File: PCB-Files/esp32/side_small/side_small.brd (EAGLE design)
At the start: 20 x 17 mm, 11 parts

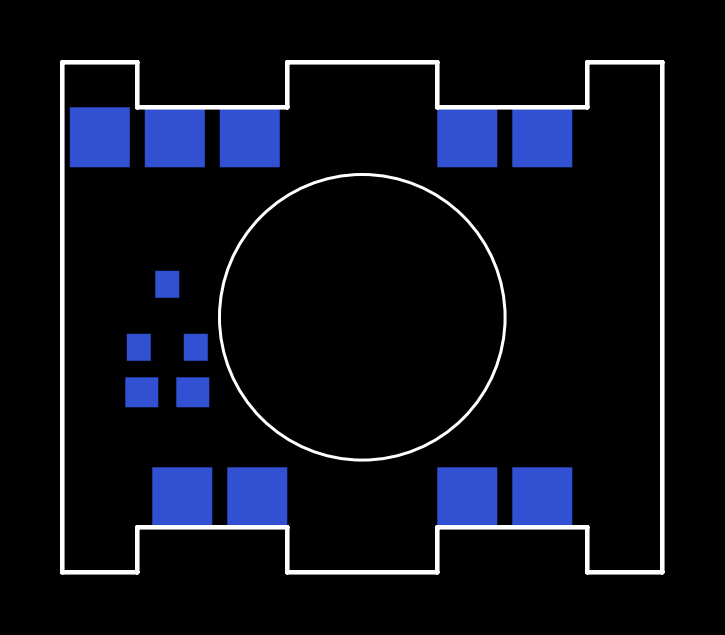
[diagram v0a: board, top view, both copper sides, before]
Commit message: basic layout; dimension for toothed joints
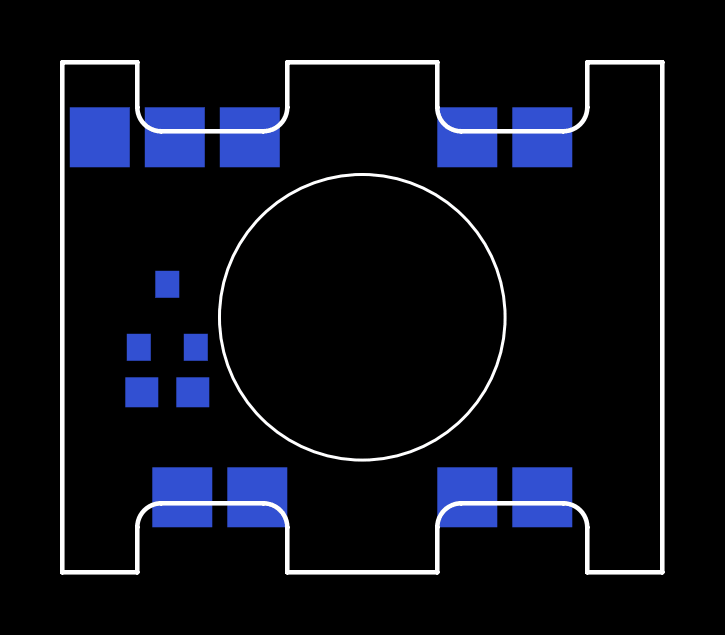
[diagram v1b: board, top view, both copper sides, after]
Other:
- outline, holes or cut-outs redrawn
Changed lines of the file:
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@@
 <board>
 <plain>
-<wire x1="35" y1="17" x2="32.5" y2="17" width="0.1524" layer="20"/>
 <circle x="25" y="8.5" radius="4.76" width="0.1" layer="20"/>
-<wire x1="27.5" y1="17" x2="22.5" y2="17" width="0.1524" layer="20"/>
-<wire x1="17.5" y1="17" x2="15" y2="17" width="0.1524" layer="20"/>
-<wire x1="17.5" y1="17" x2="17.5" y2="15.5" width="0.1524" layer="20"/>
-<wire x1="17.5" y1="15.5" x2="22.5" y2="15.5" width="0.1524" layer="20"/>
-<wire x1="22.5" y1="15.5" x2="22.5" y2="17" width="0.1524" layer="20"/>
-<wire x1="27.5" y1="17" x2="27.5" y2="15.5" width="0.1524" layer="20"/>
-<wire x1="27.5" y1="15.5" x2="32.5" y2="15.5" width="0.1524" layer="20"/>
-<wire x1="32.5" y1="15.5" x2="32.5" y2="17" width="0.1524" layer="20"/>
 <dimension x1="15" y1="17" x2="35" y2="17" x3="25" y3="18.5" textsize="1.778" layer="47"/>
 <wire x1="15" y1="17" x2="15" y2="0" width="0.1524" layer="20"/>
 <wire x1="35" y1="0" x2="35" y2="17" width="0.1524" layer="20"/>
-<wire x1="15" y1="0" x2="17.5" y2="0" width="0.1524" layer="20"/>
-<wire x1="22.5" y1="0" x2="27.5" y2="0" width="0.1524" layer="20"/>
-<wire x1="32.5" y1="0" x2="35" y2="0" width="0.1524" layer="20"/>
-<wire x1="32.5" y1="0" x2="32.5" y2="1.5" width="0.1524" layer="20"/>
-<wire x1="32.5" y1="1.5" x2="27.5" y2="1.5" width="0.1524" layer="20"/>
-<wire x1="27.5" y1="1.5" x2="27.5" y2="0" width="0.1524" layer="20"/>
-<wire x1="22.5" y1="0" x2="22.5" y2="1.5" width="0.1524" layer="20"/>
-<wire x1="22.5" y1="1.5" x2="17.5" y2="1.5" width="0.1524" layer="20"/>
-<wire x1="17.5" y1="1.5" x2="17.5" y2="0" width="0.1524" layer="20"/>
 <dimension x1="35" y1="0" x2="35" y2="17" x3="42" y3="8.5" textsize="1.778" layer="47"/>
 <dimension x1="32.5" y1="15.5" x2="32.5" y2="1.5" x3="38" y3="8.5" textsize="1.778" layer="47"/>
+<wire x1="21.7" y1="14.7" x2="18.3" y2="14.7" width="0.1524" layer="20"/>
+<wire x1="15" y1="17" x2="17.5" y2="17" width="0.1524" layer="20"/>
+<wire x1="17.5" y1="17" x2="17.5" y2="15.5" width="0.1524" layer="20"/>
+<wire x1="22.5" y1="15.5" x2="22.5" y2="17" width="0.1524" layer="20"/>
+<wire x1="22.5" y1="17" x2="27.5" y2="17" width="0.1524" layer="20"/>
+<wire x1="28.3" y1="14.7" x2="27.5" y2="15.5" width="0.1524" layer="20" curve="-90"/>
+<wire x1="27.5" y1="15.5" x2="27.5" y2="17" width="0.1524" layer="20"/>
+<wire x1="32.5" y1="17" x2="32.5" y2="15.5" width="0.1524" layer="20"/>
+<wire x1="32.5" y1="15.5" x2="31.7" y2="14.7" width="0.1524" layer="20" curve="-90"/>
+<wire x1="31.7" y1="14.7" x2="28.3" y2="14.7" width="0.1524" layer="20"/>
+<wire x1="18.3" y1="14.7" x2="17.5" y2="15.5" width="0.1524" layer="20" curve="-90"/>
+<wire x1="22.5" y1="15.5" x2="21.7" y2="14.7" width="0.1524" layer="20" curve="-90"/>
+<wire x1="32.5" y1="17" x2="35" y2="17" width="0.1524" layer="20"/>
+<wire x1="28.3" y1="2.3" x2="31.7" y2="2.3" width="0.1524" layer="20"/>
+<wire x1="35" y1="0" x2="32.5" y2="0" width="0.1524" layer="20"/>
+<wire x1="32.5" y1="0" x2="32.5" y2="1.5" width="0.1524" layer="20"/>
+<wire x1="27.5" y1="1.5" x2="27.5" y2="0" width="0.1524" layer="20"/>
+<wire x1="27.5" y1="0" x2="22.5" y2="0" width="0.1524" layer="20"/>
+<wire x1="21.7" y1="2.3" x2="22.5" y2="1.5" width="0.1524" layer="20" curve="-90"/>
+<wire x1="22.5" y1="1.5" x2="22.5" y2="0" width="0.1524" layer="20"/>
+<wire x1="17.5" y1="0" x2="17.5" y2="1.5" width="0.1524" layer="20"/>
+<wire x1="17.5" y1="1.5" x2="18.3" y2="2.3" width="0.1524" layer="20" curve="-90"/>
+<wire x1="18.3" y1="2.3" x2="21.7" y2="2.3" width="0.1524" layer="20"/>
+<wire x1="31.7" y1="2.3" x2="32.5" y2="1.5" width="0.1524" layer="20" curve="-90"/>
+<wire x1="27.5" y1="1.5" x2="28.3" y2="2.3" width="0.1524" layer="20" curve="-90"/>
+<wire x1="17.5" y1="0" x2="15" y2="0" width="0.1524" layer="20"/>
 </plain>
 <attributes>
